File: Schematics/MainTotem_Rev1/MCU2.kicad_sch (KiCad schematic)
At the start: 1 part, among them U1 STM32H757IIT6

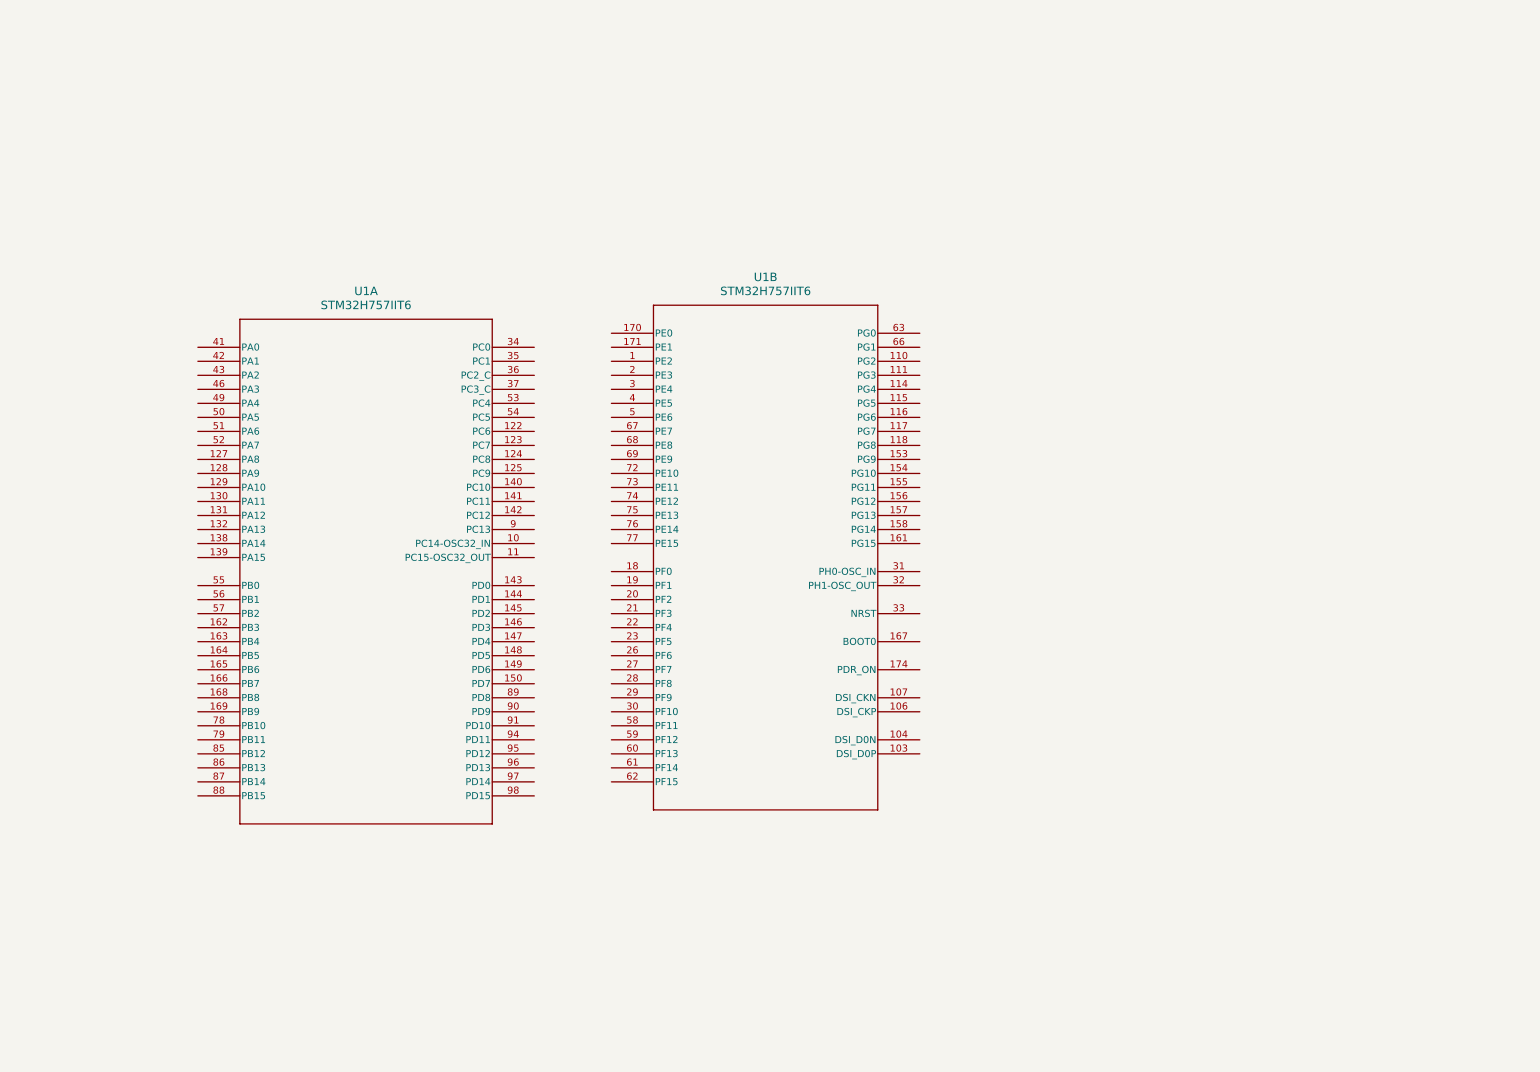
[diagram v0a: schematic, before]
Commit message: Added RS485 functionality to MainTotemLite
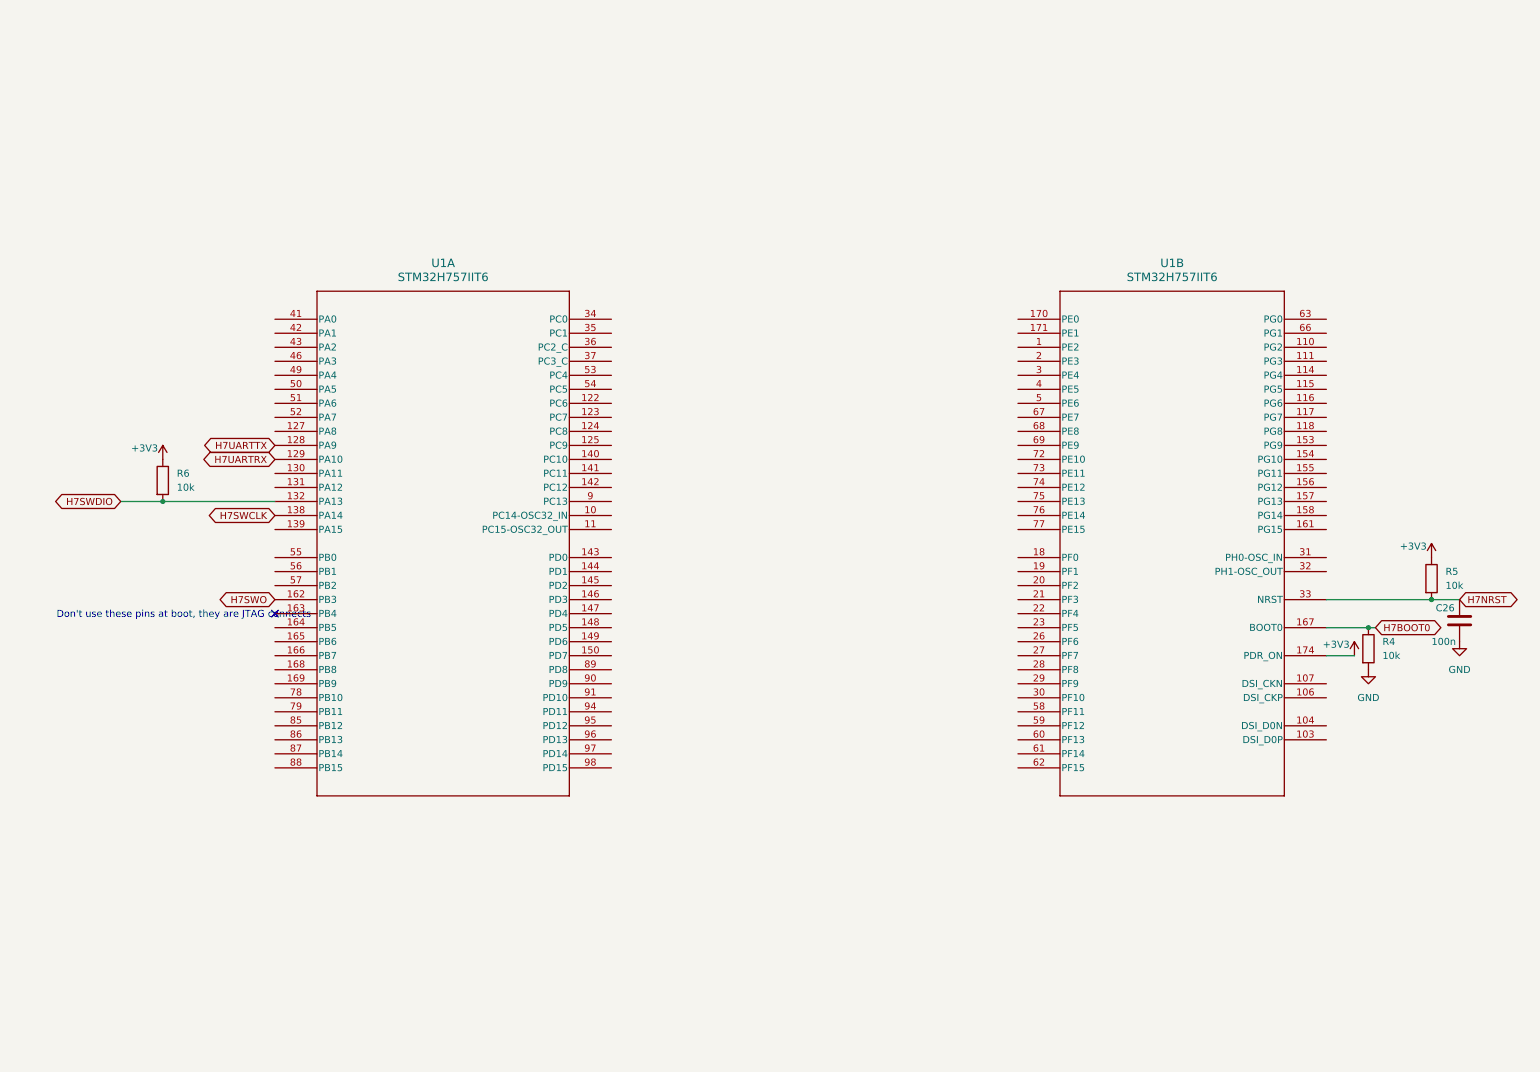
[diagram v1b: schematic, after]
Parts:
- added C26: 100n, symbol Device:C
- added R4, R5, R6: 10k, symbol Device:R
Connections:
- net H7BOOT0: now reaches U1.167 (BOOT0)
- net H7BOOT0: now also R4.1
- net +3V3: now reaches U1.174 (PDR_ON)
- net +3V3: now also R5.1, R6.1
- net H7NRST: now reaches U1.33 (NRST)
- net H7NRST: now also C26.1, R5.2
- net H7UARTTX: now reaches U1.128 (PA9)
- net H7UARTRX: now reaches U1.129 (PA10)
- net H7SWDIO: now reaches U1.132 (PA13)
- net H7SWDIO: now also R6.2
- net H7SWCLK: now reaches U1.138 (PA14)
- net H7SWO: now reaches U1.162 (PB3)
- new net GND: C26.2, R4.2
- no-connect marks 0 -> 1
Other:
- note added: "Don't use these pins at boot, they are JTAG connects"
- moved on the sheet: U1A, U1B

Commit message: Adding the MTL Schematics in post editing
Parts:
- added D2: GREEN, symbol Device:LED
- added D3: YELLOW, symbol Device:LED
- added D6: RED, symbol Device:LED
- added R17, R18, R22: 1k, symbol Device:R
- added SW3: SW_Push, symbol Switch:SW_Push
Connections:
- net +3V3: now also R17.1, R18.1, R22.1
- net GND: now also SW3.2
- net 100P_CONN/SAI1_MCLK: now reaches U1.1 (PE2)
- net 100P_CONN/GPIO_PG2: now reaches U1.110 (PG2)
- net 100P_CONN/GPIO_PG3: now reaches U1.111 (PG3)
- net 100P_CONN/GPIO_PG4: now reaches U1.114 (PG4)
- net 100P_CONN/GPIO_PG5: now reaches U1.115 (PG5)
- net 100P_CONN/GPIO_PG6: now reaches U1.116 (PG6)
- net USART6_CTS: now reaches U1.117 (PG7)
- net USART6_RTS: now reaches U1.118 (PG8)
- net at U1.153 (PG9): now also D6.1 (K)
- net at U1.154 (PG10): now also D2.1 (K)
- net at U1.155 (PG11): now also D3.1 (K)
- net at U1.156 (PG12): now also SW3.1
- net PG13: now reaches U1.157 (PG13)
- net PG14: now reaches U1.158 (PG14)
- net GPIO_PG15: now reaches U1.161 (PG15)
- net 40P_CONN/GPIO_PE0: now reaches U1.170 (PE0)
- net 40P_CONN/GPIO_PE1: now reaches U1.171 (PE1)
- net 100P_CONN/GPIO_PF0: now reaches U1.18 (PF0)
- net 100P_CONN/GPIO_PF1: now reaches U1.19 (PF1)
- net 40P_CONN/GPIO_PE3: now reaches U1.2 (PE3)
- net 100P_CONN/GPIO_PF2: now reaches U1.20 (PF2)
- net 100P_CONN/GPIO_PF3: now reaches U1.21 (PF3)
- net 100P_CONN/GPIO_PF4: now reaches U1.22 (PF4)
- net 100P_CONN/GPIO_PF5: now reaches U1.23 (PF5)
- net QSPIMEM/QUADSPI_BK1_IO3: now reaches U1.26 (PF6)
- net QSPIMEM/QUADSPI_BK1_IO2: now reaches U1.27 (PF7)
- net QSPIMEM/QUADSPI_BK1_IO0: now reaches U1.28 (PF8)
- net QSPIMEM/QUADSPI_BK1_IO1: now reaches U1.29 (PF9)
- net 100P_CONN/SAI1_FS: now reaches U1.3 (PE4)
- net QSPIMEM/QUADSPI_BK1_CLK: now reaches U1.30 (PF10)
- net OSC_IN: now reaches U1.31 (PH0-OSC_IN)
- net OSC_OUT: now reaches U1.32 (PH1-OSC_OUT)
- net 100P_CONN/SAI1_SCK: now reaches U1.4 (PE5)
- net 100P_CONN/SAI1_SD: now reaches U1.5 (PE6)
- net PF11: now reaches U1.58 (PF11)
- net PF12: now reaches U1.59 (PF12)
- net PF13: now reaches U1.60 (PF13)
- net PF14: now reaches U1.61 (PF14)
- net PF15: now reaches U1.62 (PF15)
- net 100P_CONN/GPIO_PG0: now reaches U1.63 (PG0)
- net 100P_CONN/GPIO_PG1: now reaches U1.66 (PG1)
- net 100P_CONN/GPIO_PE7: now reaches U1.67 (PE7)
- net 100P_CONN/MOTOR_CH1N: now reaches U1.68 (PE8)
- net 100P_CONN/MOTOR_CH1: now reaches U1.69 (PE9)
- net 100P_CONN/MOTOR_CH2N: now reaches U1.72 (PE10)
- net 100P_CONN/MOTOR_CH2: now reaches U1.73 (PE11)
- net 100P_CONN/MOTOR_CH3N: now reaches U1.74 (PE12)
- net 100P_CONN/MOTOR_CH3: now reaches U1.75 (PE13)
- net 100P_CONN/MOTOR_CH4: now reaches U1.76 (PE14)
- net 100P_CONN/MOTOR_BKIN: now reaches U1.77 (PE15)
- net OSC32_IN: now reaches U1.10 (PC14-OSC32_IN)
- net OSC32_OUT: now reaches U1.11 (PC15-OSC32_OUT)
- net USART6_TX: now reaches U1.122 (PC6)
- net USART6_RX: now reaches U1.123 (PC7)
- net 40P_CONN/SDMMC1_D0: now reaches U1.124 (PC8)
- net 40P_CONN/SDMMC1_D1: now reaches U1.125 (PC9)
- net 100P_CONN/GPIO_PA8_CLKOUT: now reaches U1.127 (PA8)
- net USB_D-: now reaches U1.130 (PA11)
- net USB_D+: now reaches U1.131 (PA12)
- net 40P_CONN/SDMMC1_D2: now reaches U1.140 (PC10)
- net 40P_CONN/SDMMC1_D3: now reaches U1.141 (PC11)
- net 40P_CONN/SDMMC1_CK: now reaches U1.142 (PC12)
- net 40P_CONN/FDCAN_RX: now reaches U1.143 (PD0)
- net 40P_CONN/FDCAN_TX: now reaches U1.144 (PD1)
- net 40P_CONN/SDMMC1_CMP: now reaches U1.145 (PD2)
- net 40P_CONN/USART2_CTS: now reaches U1.146 (PD3)
- net 40P_CONN/USART2_RTS: now reaches U1.147 (PD4)
- net 40P_CONN/USART2_TX: now reaches U1.148 (PD5)
- net 40P_CONN/USART2_RX: now reaches U1.149 (PD6)
- net 40P_CONN/GPIO_PD7: now reaches U1.150 (PD7)
- net 40P_CONN/I2C1_SCL: now reaches U1.168 (PB8)
- net 40P_CONN/I2C1_SDA: now reaches U1.169 (PB9)
- net 100P_CONN/ADC_PC0: now reaches U1.34 (PC0)
- net PC1: now reaches U1.35 (PC1)
- net 100P_CONN/ADC_PA0: now reaches U1.41 (PA0)
- net PA1: now reaches U1.42 (PA1)
- net PA2: now reaches U1.43 (PA2)
- net 100P_CONN/ADC_PA3: now reaches U1.46 (PA3)
- net 100P_CONN/DAC_ADC_PA4: now reaches U1.49 (PA4)
- net 100P_CONN/DAC_ADC_PA5: now reaches U1.50 (PA5)
- net 100P_CONN/ADC_PA6: now reaches U1.51 (PA6)
- net PA7: now reaches U1.52 (PA7)
- net PC4: now reaches U1.53 (PC4)
- net PC5: now reaches U1.54 (PC5)
- net 100P_CONN/ADC_PB0: now reaches U1.55 (PB0)
- net 100P_CONN/ADC_PB1: now reaches U1.56 (PB1)
- net 100P_CONN/GPIO_PB2: now reaches U1.57 (PB2)
- net PB10: now reaches U1.78 (PB10)
- net PB11: now reaches U1.79 (PB11)
- net SPI2_NSS: now reaches U1.85 (PB12)
- net SPI2_SCK: now reaches U1.86 (PB13)
- net SPI2_MISO: now reaches U1.87 (PB14)
- net SPI2_MOSI: now reaches U1.88 (PB15)
- net PD8: now reaches U1.89 (PD8)
- net PD9: now reaches U1.90 (PD9)
- net PD10: now reaches U1.91 (PD10)
- net PD11: now reaches U1.94 (PD11)
- net PD12: now reaches U1.95 (PD12)
- net PD13: now reaches U1.96 (PD13)
- net PD14: now reaches U1.97 (PD14)
- net PD15: now reaches U1.98 (PD15)
- new net: D6.2 (A), R17.2
- new net: D3.2 (A), R22.2
- new net: D2.2 (A), R18.2
- no-connect marks 1 -> 12
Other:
- added sheet 100P_CONN (100P_CONN.kicad_sch)
- added sheet 40P_CONN (40P_CONN.kicad_sch)
- added sheet QSPIMEM (QSPIMEM.kicad_sch)
- moved on the sheet: R6

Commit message: Layout Edits for Mezzanine Connector routing
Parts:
- C26: footprint (none) -> Capacitor_SMD:C_0603_1608Metric_Pad1.08x0.95mm_HandSolder
- D2, D3, D6: footprint (none) -> Resistor_SMD:R_0805_2012Metric_Pad1.20x1.40mm_HandSolder
- R17, R18, R22, R4, R5, R6: footprint (none) -> Resistor_SMD:R_0603_1608Metric_Pad0.98x0.95mm_HandSolder
- USER: renamed from SW3; footprint (none) -> Button_Switch_SMD:SW_SPST_PTS645Sx43SMTR92
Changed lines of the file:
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@@
 			)
 		)
-		(property "Footprint" ""
+		(property "Footprint" "Resistor_SMD:R_0603_1608Metric_Pad0.98x0.95mm_HandSolder"
 			(at 263.652 44.45 90)
 			(effects
@@
 			)
 		)
-		(property "Footprint" ""
+		(property "Footprint" "Resistor_SMD:R_0603_1608Metric_Pad0.98x0.95mm_HandSolder"
 			(at 271.272 62.23 90)
 			(effects
@@
 			)
 		)
-		(property "Footprint" ""
+		(property "Footprint" "Capacitor_SMD:C_0603_1608Metric_Pad1.08x0.95mm_HandSolder"
 			(at 274.0152 118.11 0)
 			(effects
@@
 			)
 		)
-		(property "Footprint" ""
+		(property "Footprint" "Resistor_SMD:R_0603_1608Metric_Pad0.98x0.95mm_HandSolder"
 			(at 267.462 53.34 90)
 			(effects
@@
 			)
 		)
-		(property "Footprint" ""
+		(property "Footprint" "Resistor_SMD:R_0603_1608Metric_Pad0.98x0.95mm_HandSolder"
 			(at 41.402 88.9 90)
 			(effects
@@
 			)
 		)
-		(property "Footprint" ""
+		(property "Footprint" "Resistor_SMD:R_0603_1608Metric_Pad0.98x0.95mm_HandSolder"
 			(at 266.192 106.68 90)
 			(effects
@@
 			)
 		)
-		(property "Footprint" ""
+		(property "Footprint" "Resistor_SMD:R_0603_1608Metric_Pad0.98x0.95mm_HandSolder"
 			(at 254.762 119.38 90)
 			(effects
@@
 			)
 		)
-		(property "Footprint" ""
+		(property "Footprint" "Resistor_SMD:R_0805_2012Metric_Pad1.20x1.40mm_HandSolder"
 			(at 265.43 52.07 0)
 			(effects
@@
 		(dnp no)
 		(fields_autoplaced yes)
-		(property "Reference" "SW3"
+		(property "Reference" "USER"
 			(at 278.13 82.55 0)
 			(effects
@@
 			)
 		)
-		(property "Footprint" ""
+		(property "Footprint" "Button_Switch_SMD:SW_SPST_PTS645Sx43SMTR92"
 			(at 278.13 85.09 0)
 			(effects
@@
 			(project ""
 				(path "/f88ba0f4-041f-4cf3-b904-3ea5c6101abb/39b009e0-d9eb-493f-99f5-9b2cb61eab22"
-					(reference "SW3")
+					(reference "USER")
 					(unit 1)
 				)
@@
 			)
 		)
-		(property "Footprint" ""
+		(property "Footprint" "Resistor_SMD:R_0805_2012Metric_Pad1.20x1.40mm_HandSolder"
 			(at 273.05 69.85 0)
 			(effects
@@
 			)
 		)
-		(property "Footprint" ""
+		(property "Footprint" "Resistor_SMD:R_0805_2012Metric_Pad1.20x1.40mm_HandSolder"
 			(at 269.24 60.96 0)
 			(effects

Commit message: Rerouting layout to resolve collision issues
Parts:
- renumbered USER to USER1
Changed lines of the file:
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@@
 		(dnp no)
 		(fields_autoplaced yes)
-		(property "Reference" "USER"
+		(property "Reference" "USER1"
 			(at 278.13 82.55 0)
 			(effects
@@
 			(project ""
 				(path "/f88ba0f4-041f-4cf3-b904-3ea5c6101abb/39b009e0-d9eb-493f-99f5-9b2cb61eab22"
-					(reference "USER")
+					(reference "USER1")
 					(unit 1)
 				)
